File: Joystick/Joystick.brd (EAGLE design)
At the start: 36.3 x 29.8 mm, 11 parts

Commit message: Checkpointing PCB designs
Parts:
- removed B1, B3, B4, B5, B7: TACT-SWITCH, IntegerLabs:MJTP1138
- removed R1: 680, SparkFun-Passives:0805
- added U1: JOYSTICKPTH, IntegerLabs:JOYSTICK
- R2: value 1 -> 680; device SparkFun-Resistors:0805 -> SparkFun-Passives:0805
- moved R2 18.6 mm to (24.4, 15.2), flipped to the bottom, turned to 270 degrees
- moved U$1 15.1 mm to (19.4, 17.8), flipped to the bottom
- moved C1 9.34 mm to (19.7, 20.3), flipped to the bottom
- renumbered U$2 to U$7
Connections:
- removed net BUTTON0: B5.POS1, U$1.13
- removed net BUTTON1: B1.POS1, U$1.12
- removed net BUTTON2: B3.POS1, U$1.11
- removed net BUTTON3: B7.POS2, U$1.10
- removed net BUTTON4: B4.POS1, U$1.2
- removed net N$2: R2.2, U$7.BUS2
- removed net N$8: LED1.A, R1.1
- new net H: U$1.13, U1.H2
- new net N$7: LED1.A, R2.1
- new net SEL: U$1.11, U1.B1A
- new net V: U$1.12, U1.V2
- net GND: now also U1.B2A, U1.H3, U1.V3; no longer B1.NEG2, B3.NEG2, B4.NEG2, B5.NEG2, B7.NEG2
- net LED: now also R2.2; no longer R1.2
- net VCC: now also U$7.BUS2, U1.H1, U1.V1; no longer R2.1
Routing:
- net LED: track 56.8 -> 4.52 mm, vias 2 -> 0
- net SEL: track 0.00 -> 35.9 mm
- net BUTTON0: track 34.7 -> 0.00 mm
- net BUTTON4: track 31.8 -> 0.00 mm
- net BUTTON3: track 30.1 -> 0.00 mm
- net VCC: track 46.4 -> 69.5 mm, vias 1 -> 2
- net N$7: track 0.00 -> 15.2 mm, vias 0 -> 1
- net GND: track 23.4 -> 8.31 mm, vias 7 -> 2
- net BUTTON2: track 14.1 -> 0.00 mm, vias 2 -> 0
- net H: track 0.00 -> 11.2 mm
- net V: track 0.00 -> 11.1 mm, vias 0 -> 1
- net SDA/MOSI: track 55.6 -> 45.8 mm, vias 1 -> 0
- net N$2: track 8.52 -> 0.00 mm, vias 1 -> 0
- net RESET: track 16.9 -> 22.6 mm, vias 1 -> 2
- net SCL/SCK: track 28.5 -> 23.7 mm, vias 2 -> 0
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- added copper zone on layer 1, net GND
- removed copper zone on layer 16, net GND
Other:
- board text removed: "0"
- board text removed: "1"
- board text removed: "2"
- board text removed: "3"
- board text removed: "4"

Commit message: Various updates
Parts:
- removed R2: 680, SparkFun-Passives:0805
- removed U$1: TINY841, IntegerLabs:SOIC14
- added R1: 681Ω, Modulo:0603
- added U2: ATTINY841, Modulo:SOIC-14
- C1: value .47uF -> 100nF; device SparkFun-Capacitors:0805 -> Modulo:0603
- LED1: value (none) -> blue; device adafruit:CHIP-LED0805 -> Modulo:0805-LED
- U$7: value FOOTPRINTFOOTPRINT-2 -> DEVICE-PCB-TABS; device IntegerLabs:FOOTPRINT2 -> Modulo:DEVICE-PCB-TABS
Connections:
- net GND: now also U2.14; no longer U$1.14
- net H: now also U2.13; no longer U$1.13
- net LED: now also R1.2, U2.6; no longer R2.2, U$1.6
- net MISO: now also U2.8; no longer U$1.8
- net N$7: now also R1.1; no longer R2.1
- net RESET: now also U2.4; no longer U$1.4
- net SCL/SCK: now also U2.9; no longer U$1.9
- net SDA/MOSI: now also U2.7; no longer U$1.7
- net SEL: now also U2.11; no longer U$1.11
- net V: now also U2.12; no longer U$1.12
- net VCC: now also U2.1; no longer U$1.1
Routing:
- net VCC: track 69.5 -> 70.0 mm
- net SCL/SCK: track 23.7 -> 24.0 mm, vias 0 -> 2
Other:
- outline, holes or cut-outs redrawn

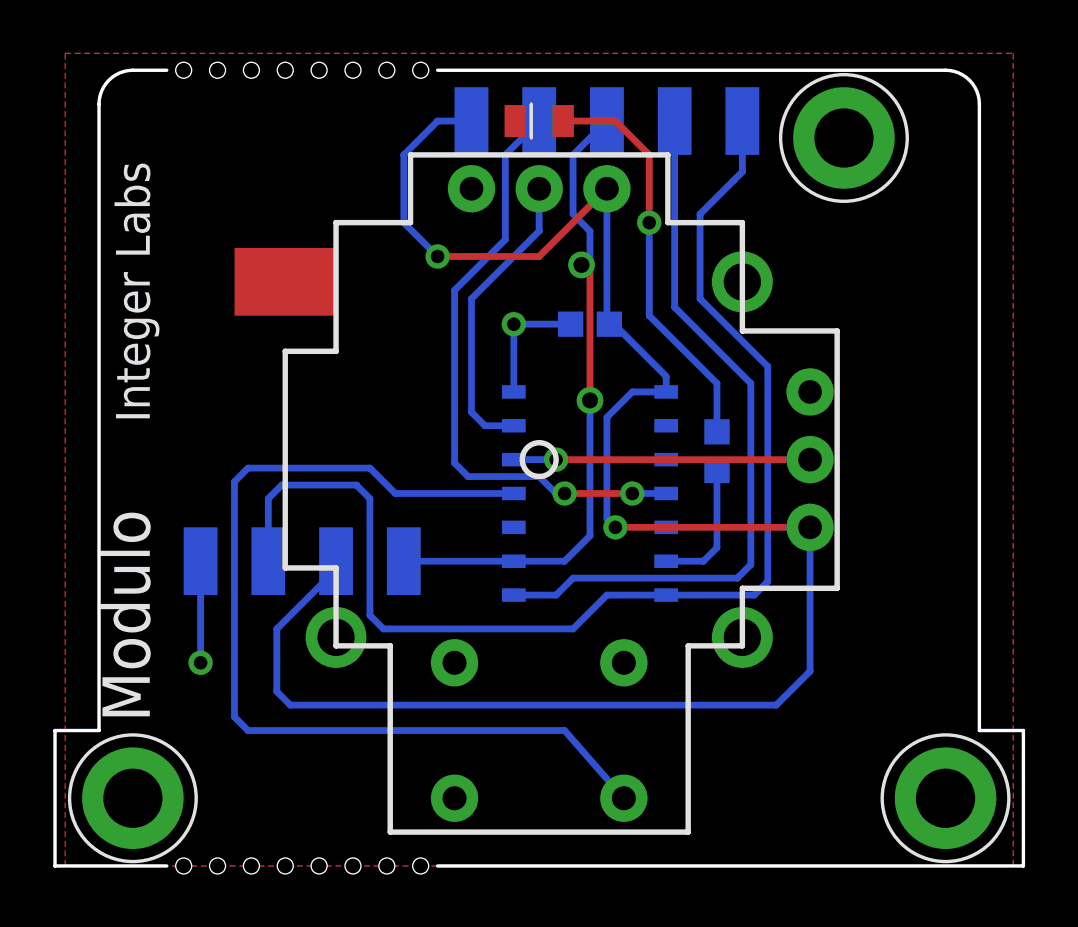
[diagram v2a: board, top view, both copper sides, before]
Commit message: Major revision of all boards. Cleaned up old files. Exported BOM csv files for all boards
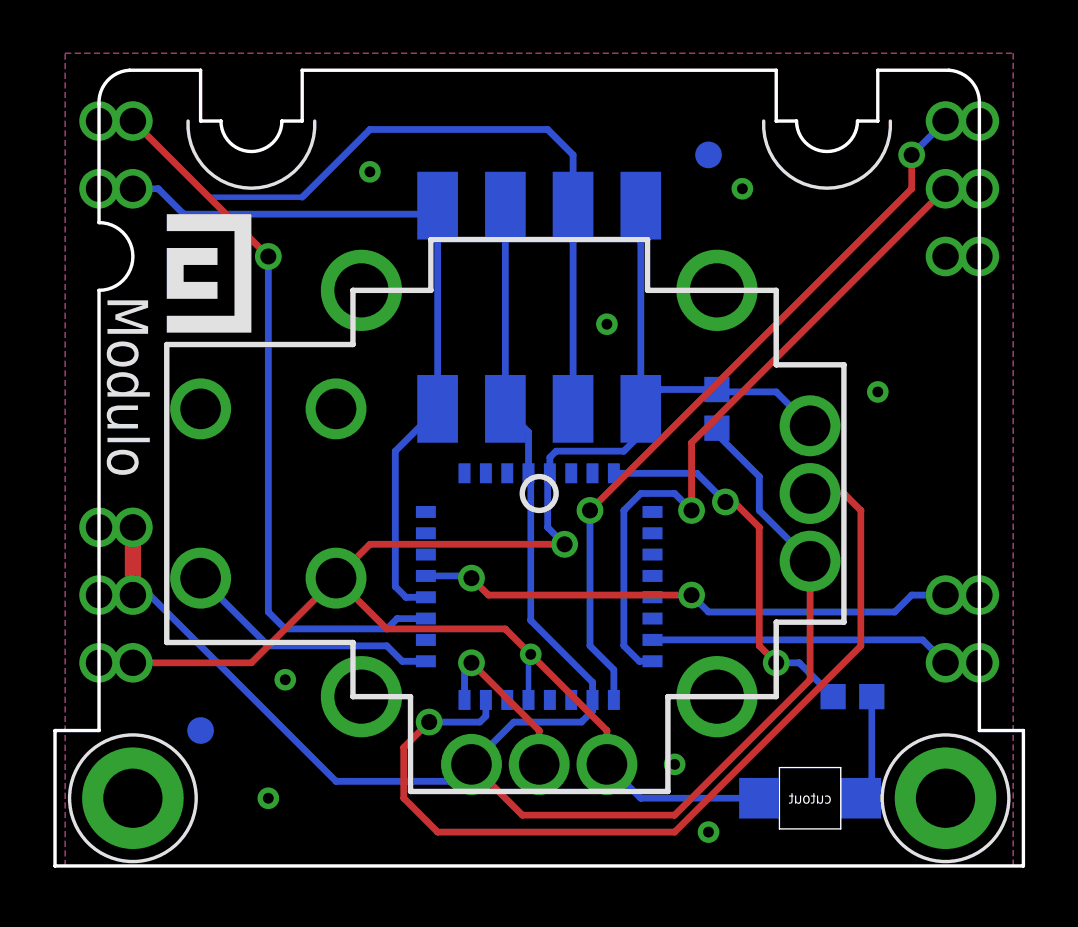
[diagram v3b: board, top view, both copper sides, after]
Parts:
- removed U$7: DEVICE-PCB-TABS, Modulo:DEVICE-PCB-TABS
- added F1, F2: FIDUCIAL, Modulo:FIDUCIAL_1MM
- added JP1: HEADER-1X4-AMPMODU, Modulo:AMPMODU-4P
- added PCB1: DEVICE-PCB, Modulo:DEVICE-PCB
- added U$1, U$2: (no value), Modulo:LOGO-SMALL
- C1: value 100nF -> .1uF
- LED1: value blue -> LED-1206-REV; device Modulo:0805-LED -> Modulo:LED-1206-REV
- R1: value 681Ω -> 1KΩ
- U1: value JOYSTICKPTH -> ATTINY48/88-TQFP; device IntegerLabs:JOYSTICK -> Modulo:TQFP-32
- U2: value ATTINY841 -> JOYSTICK; device Modulo:SOIC-14 -> Modulo:JOYSTICK
- moved LED1 27.4 mm to (27.9, 2.54), flipped to the bottom, turned to 0 degrees
- moved R1 10.5 mm to (29.5, 6.35), turned to 0 degrees
- moved C1 5.72 mm to (24.4, 17.1), turned to 90 degrees
- moved U1 4.76 mm to (17.8, 10.5), flipped to the bottom, turned to 270 degrees
- moved U2 4.13 mm to (17.8, 14.0), flipped to the top, turned to 90 degrees
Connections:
- removed net SCL/SCK: U$7.BUS3, U$7.PROG2, U2.9
- removed net SDA/MOSI: U$7.BUS1, U$7.PROG4, U2.7
- new net MOSI: PCB1.MOSI, U1.15
- new net SCK: PCB1.CLK, U1.17
- new net SCL: JP1.P$7, JP1.P$8, PCB1.SCL, U1.28
- new net SDA: JP1.P$3, JP1.P$4, PCB1.SDA, U1.27
- net GND: now also C1.2, JP1.P$1, JP1.P$2, PCB1.GND, U1.21, U1.5, U2.B2A, U2.H3, U2.V3; no longer C1.1, U$7.BUS0, U1.B2A, U1.H3, U1.V3, U2.14
- net H: now also U1.23, U2.H2; no longer U1.H2, U2.13
- net LED: now also U1.8; no longer U2.6
- net MISO: now also PCB1.MISO, U1.16; no longer U$7.PROG3, U2.8
- net RESET: now also PCB1.RESET, U1.29; no longer U$7.PROG1, U2.4
- net SEL: now also U1.25, U2.B1A; no longer U1.B1A, U2.11
- net V: now also U1.24, U2.V2; no longer U1.V2, U2.12
- net VCC: now also C1.1, JP1.P$5, JP1.P$6, PCB1.VCC, PCB1.VPROG, U1.18, U1.4, U2.H1, U2.V1; no longer C1.2, U$7.BUS2, U$7.PROG0, U1.H1, U1.V1, U2.1
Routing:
- net SDA: track 0.00 -> 55.5 mm, vias 0 -> 1
- net GND: track 8.48 -> 62.9 mm, vias 2 -> 10
- net SDA/MOSI: track 45.8 -> 0.00 mm
- net SCL: track 0.00 -> 28.2 mm
- net SCK: track 0.00 -> 27.6 mm, vias 0 -> 2
- net SEL: track 35.9 -> 9.74 mm
- net SCL/SCK: track 24.0 -> 0.00 mm, vias 2 -> 0
- net H: track 11.2 -> 33.9 mm, vias 0 -> 1
- net MOSI: track 0.00 -> 11.3 mm
- net N$1: track 15.2 -> 3.98 mm, vias 1 -> 0
- net LED: track 5.01 -> 14.3 mm, vias 0 -> 2
- net V: track 11.1 -> 6.36 mm
- net RESET: track 22.6 -> 20.3 mm
- net MISO: track 27.2 -> 25.5 mm, vias 0 -> 1
- net VCC: track 70.0 -> 70.5 mm, vias 2 -> 0
- added copper zone on layer 16, net GND
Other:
- outline, holes or cut-outs redrawn

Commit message: Check point of current PCB designs. Among other things I think this change includes rewiring of programming lines on many of the boards,.
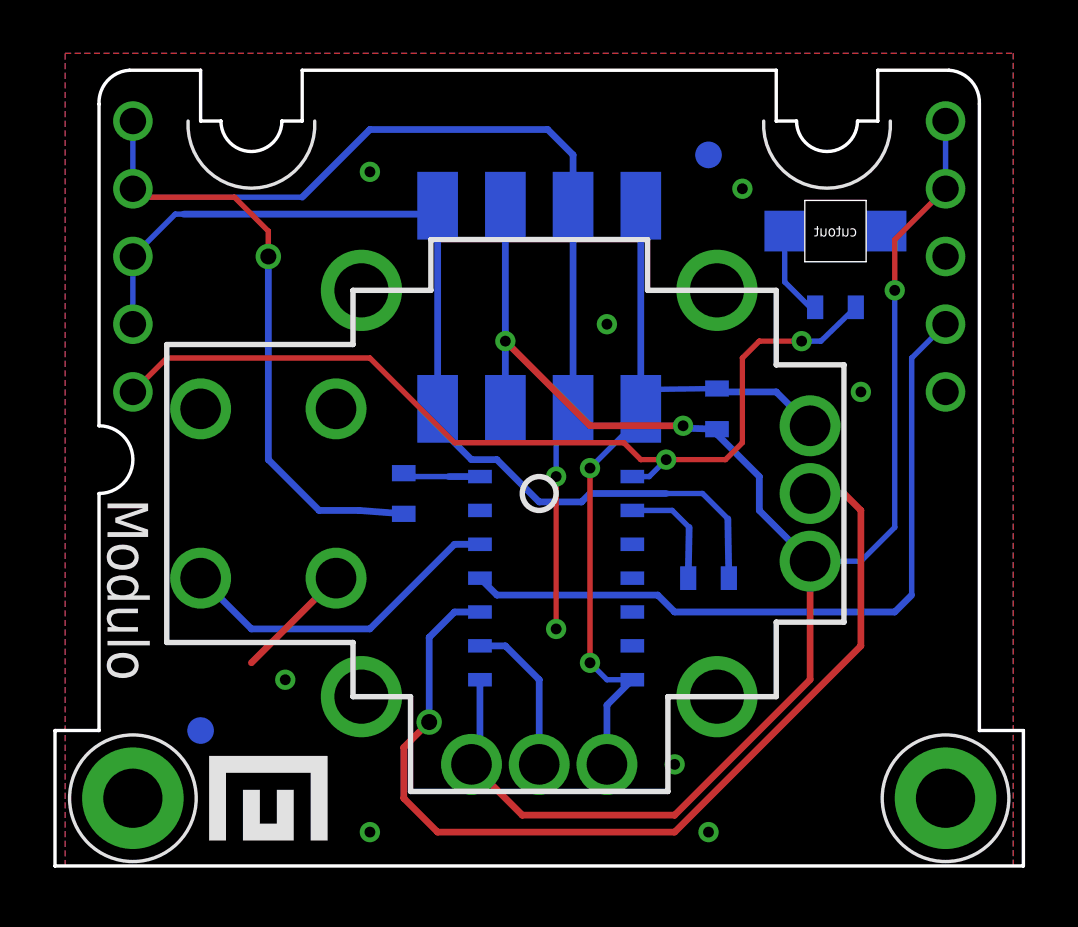
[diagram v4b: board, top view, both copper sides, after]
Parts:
- removed U1: ATTINY48/88-TQFP, Modulo:TQFP-32
- added R8, R9: 150Ω, Modulo:0603
- added U3: ATTINY841, Modulo:SOIC-14
- moved LED1 21.3 mm to (28.9, 23.8), turned to 180 degrees
- moved U$2 21.1 mm to (7.30, 1.59), turned to 0 degrees
- moved U$1 19.7 mm to (28.3, 1.59), turned to 0 degrees
- moved R1 14.6 mm to (28.9, 21.0), turned to 180 degrees
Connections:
- removed net LED: R1.2, U1.8
- removed net MISO: PCB1.MISO, U1.16
- removed net MOSI: PCB1.MOSI, U1.15
- removed net SCK: PCB1.CLK, U1.17
- new net MISO/LED: PCB1.MISO, R1.2, U3.8
- new net SCL/SCK: R8.2, U3.9
- new net SDA/MOSI: R9.2, U3.7
- net GND: now also U3.14; no longer U1.21, U1.5
- net H: now also U3.3; no longer U1.23
- net RESET: now also U3.4; no longer U1.29
- net SCL: now also PCB1.CLK, R8.1; no longer U1.28
- net SDA: now also PCB1.MOSI, R9.1; no longer U1.27
- net SEL: now also U3.5; no longer U1.25
- net V: now also U3.2; no longer U1.24
- net VCC: now also U3.1; no longer U1.18, U1.4
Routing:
- net MISO/LED: track 0.00 -> 35.0 mm, vias 0 -> 2
- net GND: track 62.9 -> 35.2 mm
- net SCK: track 27.6 -> 0.00 mm, vias 2 -> 0
- net MISO: track 25.5 -> 0.00 mm, vias 1 -> 0
- net LED: track 14.3 -> 0.00 mm, vias 2 -> 0
- net MOSI: track 11.3 -> 0.00 mm
- net SCL: track 28.2 -> 37.8 mm
- net RESET: track 20.3 -> 27.7 mm, vias 2 -> 0
- net SCL/SCK: track 0.00 -> 4.30 mm
- net VCC: track 70.5 -> 66.4 mm, vias 0 -> 3
- net SDA: track 55.5 -> 59.0 mm, vias 1 -> 3
- net SDA/MOSI: track 0.00 -> 2.92 mm
- net SEL: track 9.74 -> 12.6 mm
- net H: track 33.9 -> 36.5 mm
- net N$1: track 3.98 -> 3.44 mm
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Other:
- outline, holes or cut-outs redrawn

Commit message: Moved logo near LED Bumped version number Increased trace widths from 8mil to 10mil tented vias
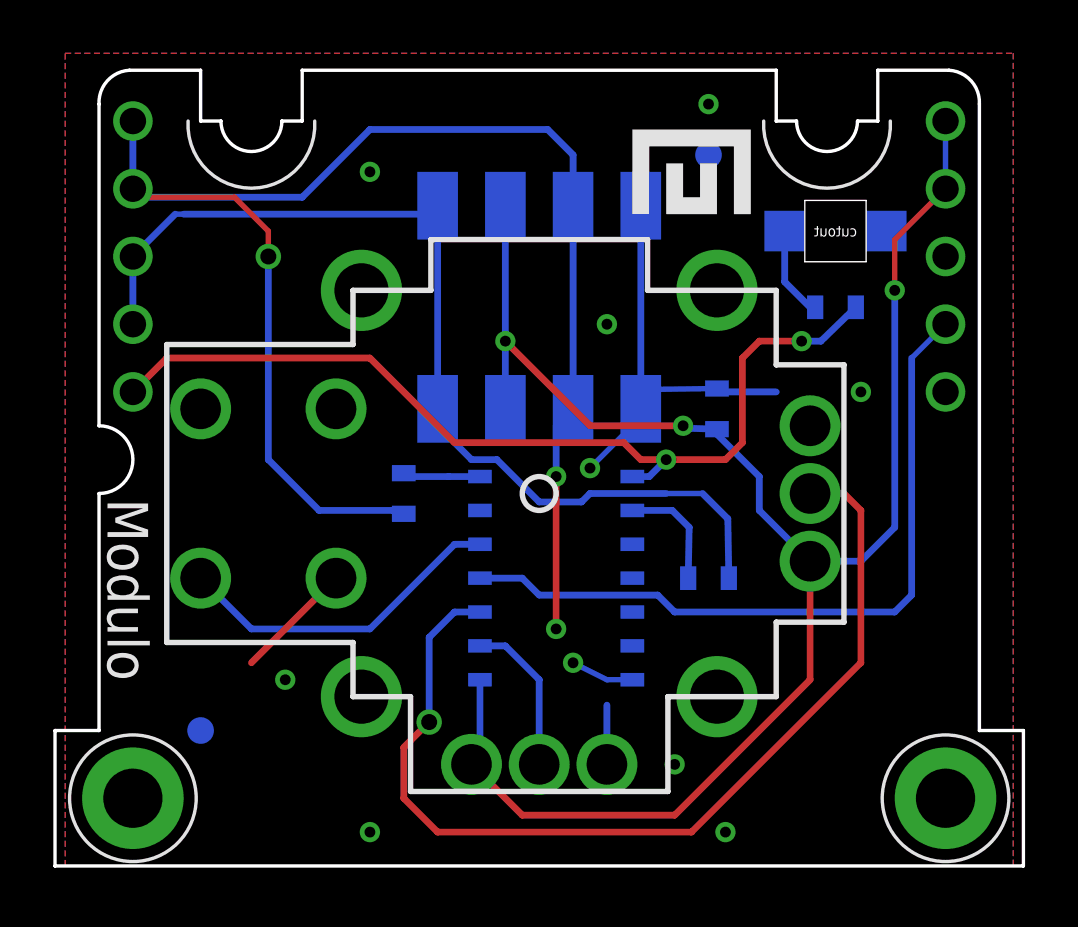
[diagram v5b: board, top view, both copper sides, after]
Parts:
- moved U$2 28.4 mm to (23.2, 25.1)
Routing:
- net GND: track 35.2 -> 25.3 mm

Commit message: Various changes
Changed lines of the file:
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@@
 <wire x1="6.985" y1="7.62" x2="10.16" y2="10.795" width="0.254" layer="1"/>
 <wire x1="26.67" y1="17.78" x2="24.5375" y2="17.78" width="0.254" layer="16"/>
-<wire x1="24.5375" y1="17.78" x2="24.4475" y2="17.907" width="0.254" layer="16"/>
+<wire x1="24.5375" y1="17.78" x2="24.4475" y2="17.9832" width="0.254" layer="16"/>
 <wire x1="21.59" y1="24.765" x2="21.59" y2="17.78" width="0.254" layer="16"/>
 <wire x1="21.59" y1="17.78" x2="21.59" y2="17.145" width="0.254" layer="16"/>
@@
 <wire x1="21.59" y1="16.1925" x2="20.955" y2="16.1925" width="0.2032" layer="16"/>
 <wire x1="20.955" y1="16.1925" x2="19.685" y2="14.9225" width="0.2032" layer="16"/>
-<wire x1="24.4475" y1="17.907" x2="21.68" y2="17.87" width="0.2032" layer="16"/>
+<wire x1="24.4475" y1="17.9832" x2="21.68" y2="17.87" width="0.2032" layer="16"/>
 <wire x1="21.68" y1="17.87" x2="21.59" y2="17.78" width="0.2032" layer="16"/>
 </signal>
@@
 <wire x1="22.86" y1="1.905" x2="17.145" y2="1.905" width="0.254" layer="1"/>
 <wire x1="17.145" y1="1.905" x2="15.24" y2="3.81" width="0.254" layer="1"/>
-<wire x1="24.4475" y1="16.383" x2="24.4475" y2="16.1925" width="0.254" layer="16"/>
+<wire x1="24.4475" y1="16.3068" x2="24.4475" y2="16.1925" width="0.254" layer="16"/>
 <wire x1="24.4475" y1="16.1925" x2="26.035" y2="14.605" width="0.254" layer="16"/>
 <wire x1="26.035" y1="14.605" x2="26.035" y2="13.335" width="0.254" layer="16"/>
@@
 <wire x1="15.5575" y1="6.985" x2="15.5575" y2="4.1275" width="0.254" layer="16"/>
 <wire x1="15.5575" y1="4.1275" x2="15.24" y2="3.81" width="0.254" layer="16"/>
-<wire x1="24.4475" y1="16.383" x2="23.2675" y2="16.42" width="0.254" layer="16"/>
+<wire x1="24.4475" y1="16.3068" x2="23.2675" y2="16.42" width="0.254" layer="16"/>
 <wire x1="23.2675" y1="16.42" x2="23.1775" y2="16.51" width="0.254" layer="16"/>
 <via x="23.1775" y="16.51" extent="1-16" drill="0.4064"/>
@@
 <contactref element="R1" pad="1"/>
 <contactref element="LED1" pad="A"/>
-<wire x1="28.1305" y1="20.955" x2="27.94" y2="20.955" width="0.2032" layer="16"/>
+<wire x1="28.0543" y1="20.955" x2="27.94" y2="20.955" width="0.2032" layer="16"/>
 <wire x1="27.94" y1="20.955" x2="26.9875" y2="21.9075" width="0.254" layer="16"/>
-<wire x1="26.9875" y1="21.9075" x2="26.9875" y2="23.8125" width="0.254" layer="16"/>
+<wire x1="26.9875" y1="21.9075" x2="27.1145" y2="23.8125" width="0.254" layer="16"/>
 </signal>
 <signal name="SCL">
@@
 <wire x1="13.6525" y1="24.4475" x2="13.97" y2="24.765" width="0.254" layer="16"/>
 <contactref element="R8" pad="1"/>
-<wire x1="24.892" y1="10.795" x2="24.855" y2="13.0219" width="0.254" layer="16"/>
+<wire x1="24.9682" y1="10.795" x2="24.855" y2="13.0219" width="0.254" layer="16"/>
 <wire x1="22.5425" y1="13.97" x2="19.685" y2="13.97" width="0.254" layer="16"/>
 <wire x1="19.685" y1="13.97" x2="19.3675" y2="13.6525" width="0.254" layer="16"/>
@@
 <wire x1="7.62" y1="15.24" x2="9.525" y2="13.335" width="0.254" layer="16"/>
 <wire x1="9.525" y1="13.335" x2="12.2925" y2="13.335" width="0.254" layer="16"/>
-<wire x1="12.2925" y1="13.335" x2="12.7" y2="13.208" width="0.254" layer="16"/>
+<wire x1="12.2925" y1="13.335" x2="12.7" y2="13.1318" width="0.254" layer="16"/>
 <contactref element="PCB1" pad="MOSI"/>
 <via x="18.415" y="8.89" extent="1-16" drill="0.4064"/>
@@
 <wire x1="6.35" y1="25.0825" x2="2.8575" y2="25.0825" width="0.2032" layer="1"/>
 <wire x1="2.8575" y1="25.0825" x2="2.54" y2="25.4" width="0.2032" layer="1"/>
-<wire x1="12.7" y1="13.208" x2="12.7" y2="13.335" width="0.2032" layer="16"/>
+<wire x1="12.7" y1="13.1318" x2="12.7" y2="13.335" width="0.2032" layer="16"/>
 </signal>
 <signal name="SCL/SCK">
 <contactref element="R8" pad="2"/>
 <contactref element="U3" pad="9"/>
-<wire x1="23.368" y1="10.795" x2="23.405" y2="12.7" width="0.254" layer="16"/>
+<wire x1="23.2918" y1="10.795" x2="23.405" y2="12.7" width="0.254" layer="16"/>
 <wire x1="21.2725" y1="13.335" x2="22.77" y2="13.335" width="0.254" layer="16"/>
 <wire x1="22.77" y1="13.335" x2="23.405" y2="12.7" width="0.254" layer="16"/>
@@
 <wire x1="15.5575" y1="14.605" x2="14.3819" y2="14.605" width="0.254" layer="16"/>
 <wire x1="14.3819" y1="14.605" x2="12.79" y2="14.605" width="0.254" layer="16"/>
-<wire x1="12.79" y1="14.605" x2="12.7" y2="14.732" width="0.2032" layer="16"/>
+<wire x1="12.79" y1="14.605" x2="12.7" y2="14.8082" width="0.2032" layer="16"/>
 </signal>
 <signal name="MISO/LED">
@@
 <via x="27.6225" y="19.685" extent="1-16" drill="0.4064"/>
 <wire x1="27.6225" y1="19.685" x2="28.3475" y2="19.685" width="0.254" layer="16"/>
-<wire x1="28.3475" y1="19.685" x2="29.6545" y2="20.955" width="0.254" layer="16"/>
+<wire x1="28.3475" y1="19.685" x2="29.7307" y2="20.955" width="0.254" layer="16"/>
 <wire x1="22.5425" y1="15.24" x2="21.59" y2="15.24" width="0.254" layer="1"/>
 <wire x1="21.59" y1="15.24" x2="20.955" y2="15.875" width="0.254" layer="1"/>
